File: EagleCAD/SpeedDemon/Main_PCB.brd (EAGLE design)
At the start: 77 x 46.5 mm, 65 parts, among them Q1 DMC2700, U3 LM3676, U4 STM32F072-LQFP48, X1 32.768kHz

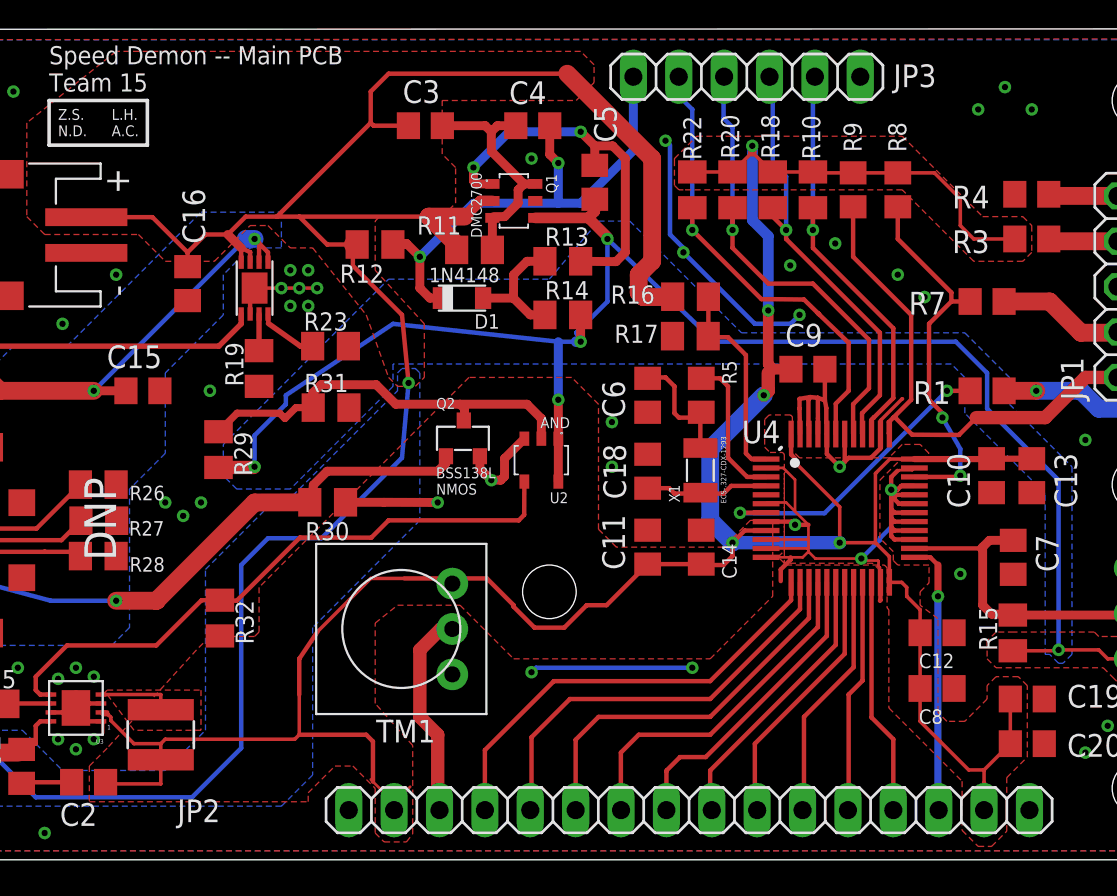
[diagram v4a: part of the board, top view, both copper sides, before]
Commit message: updated schematic/layout with pwr inlet debounce circuit and added center switch connectivity to MCU. Other small organizational changes.
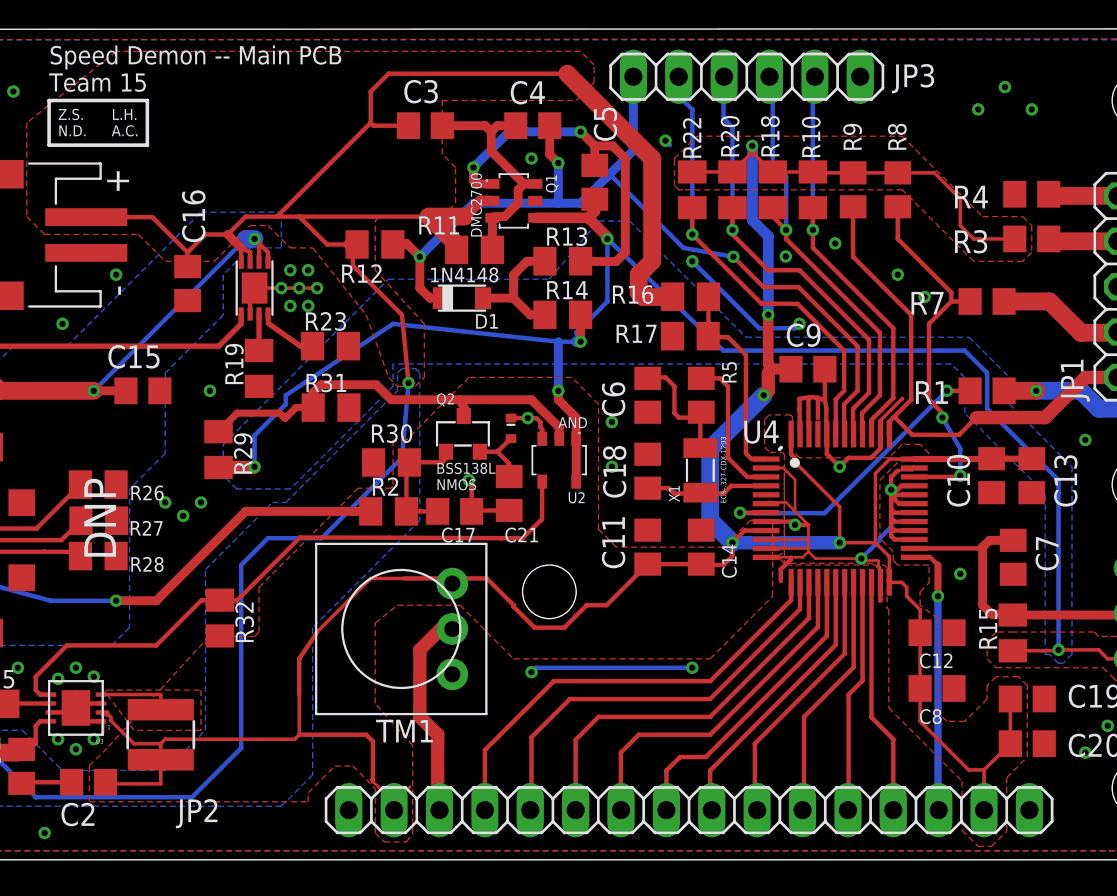
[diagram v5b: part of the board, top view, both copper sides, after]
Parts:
- added C17: 10uF, 0805_generics:C_0805
- added C21: 4.7uF, 0805_generics:C_0805
- added D3: (no value), LCRD_SMD_generics:SOD-882
- added R2: 22k, 0805_generics:R_0805
- R30: value 10k -> 82k
- moved R30 4.21 mm to (31.2, 22.2), turned to 180 degrees
- moved U2 1.00 mm to (40.5, 22.4)
- moved Q2 0.25 mm to (35.2, 23.8)
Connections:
- new net N$12: C17.1, Q2.1, R2.2, R30.1
- new net N$16: C21.1, D3.P$1, Q2.2
- net +V+_CHG: now also R2.1; no longer Q2.1, R30.1
- net GND: now also C17.2, C21.2, D3.P$2; no longer Q2.2, U4.42
- net PWR_SW: now also U4.42
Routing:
- net PWR_SW: track 28.1 -> 51.1 mm, vias 2 -> 3
- net GND: track 113.4 -> 99.9 mm
- net N$12: track 0.00 -> 7.08 mm
- net +V+_CHG: track 71.8 -> 65.7 mm
- net N$16: track 0.00 -> 3.70 mm
- net +3V3: track 163.8 -> 165.1 mm
- net BATT_CHG_LOGIC_OP: track 34.7 -> 35.8 mm
- net N$28: track 22.9 -> 23.9 mm

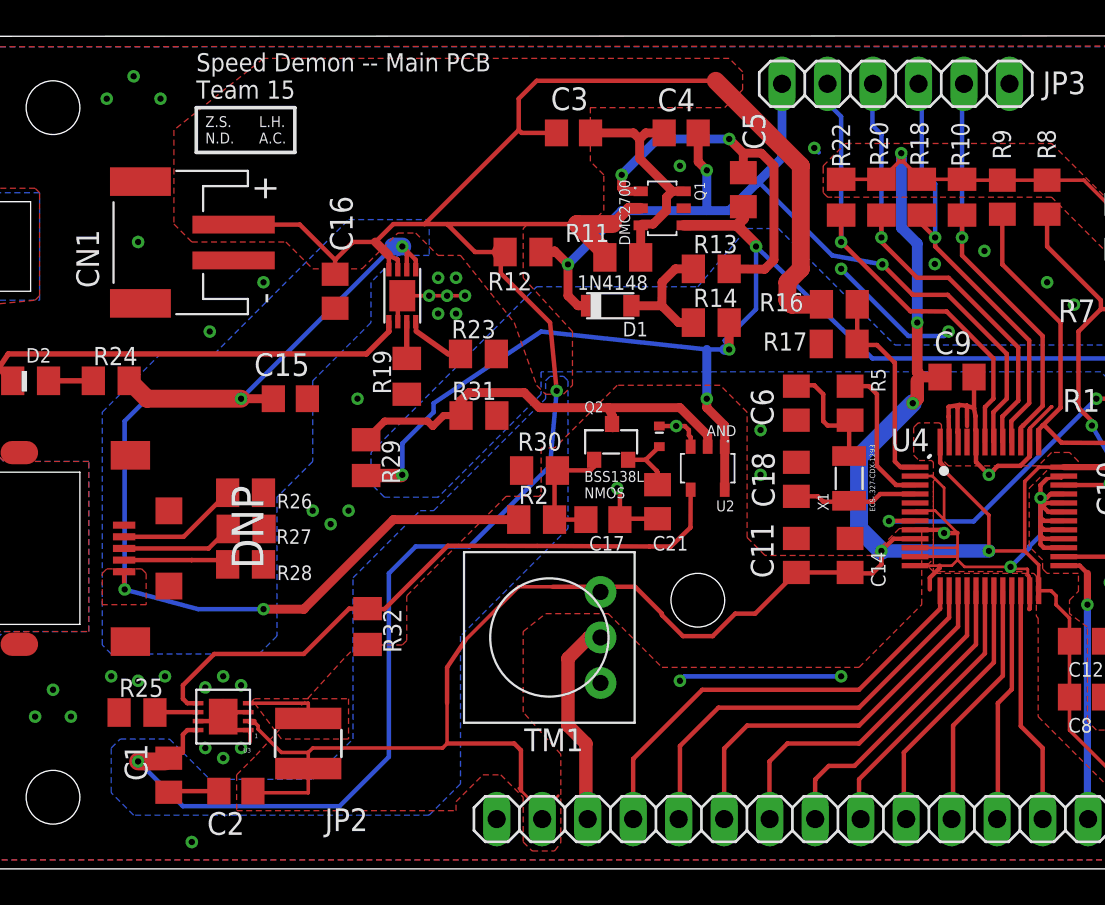
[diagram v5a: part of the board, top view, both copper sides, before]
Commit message: Changed layout to maximize distance between power inductor and everything else
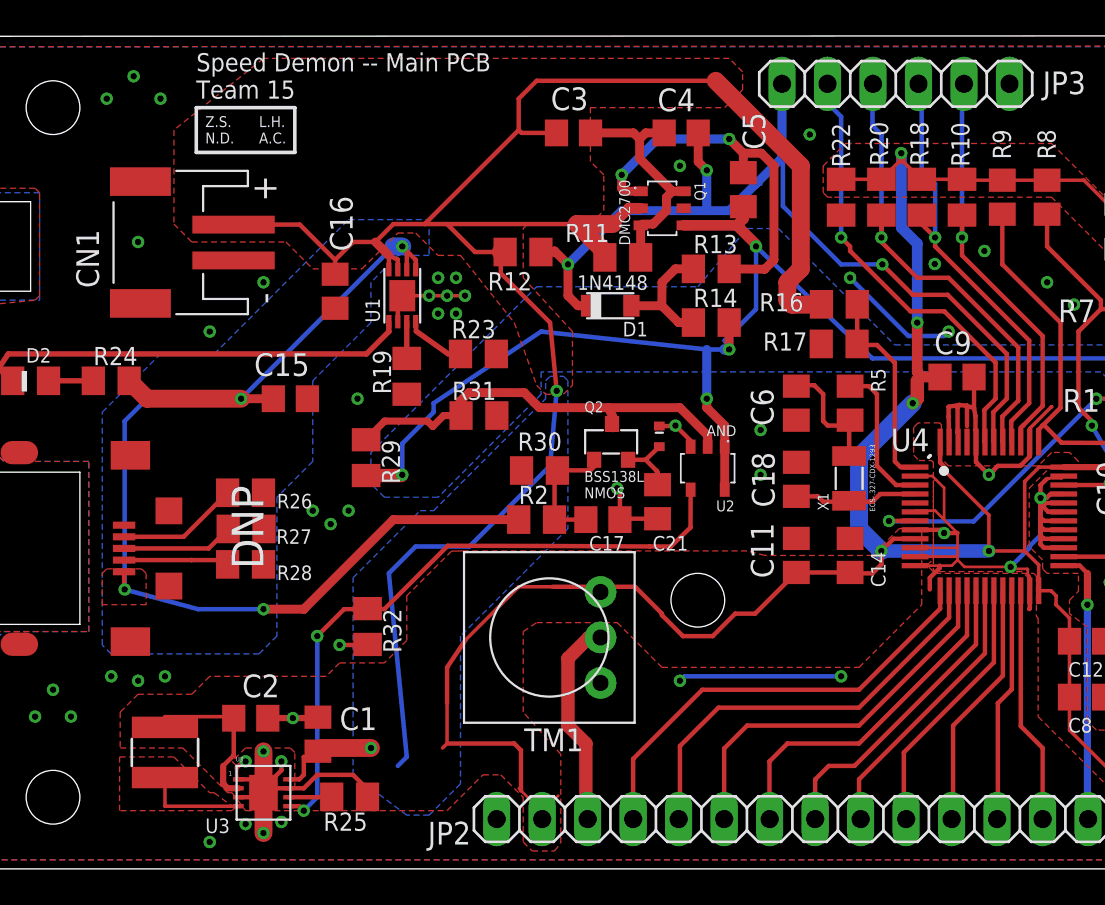
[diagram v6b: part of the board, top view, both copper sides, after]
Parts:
- moved R25 12.8 mm to (20.6, 4.02), turned to 180 degrees
- moved C1 8.64 mm to (18.8, 7.52), turned to 90 degrees
- moved L1 8.02 mm to (10.2, 6.50), turned to 270 degrees
- moved U3 4.81 mm to (15.8, 4.25), turned to 0 degrees
- moved C2 4.15 mm to (15.0, 8.41), turned to 0 degrees
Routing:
- net VBATT+: track 129.9 -> 115.7 mm
- net GND: track 99.9 -> 113.1 mm, vias 56 -> 58
- net +3V3: track 165.1 -> 157.4 mm
- net SW_LEFT: track 28.7 -> 25.3 mm
- net N$10: track 4.20 -> 5.70 mm
- net PWR_SW: track 51.1 -> 52.2 mm
- net BATT_CHG_LOGIC_OP: track 35.8 -> 36.5 mm, vias 0 -> 2
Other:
- board text added: "U1"
- board text added: "U3"

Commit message: several small changes to layout to improve ground planing
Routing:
- net GND: vias 58 -> 61
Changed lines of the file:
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@@
 <setting verticaltext="up"/>
 </settings>
-<grid distance="0.25" unitdist="mm" unit="mm" style="lines" multiple="1" display="yes" altdistance="0.003125" altunitdist="mic" altunit="mm"/>
+<grid distance="0.25" unitdist="mm" unit="mm" style="lines" multiple="1" display="no" altdistance="0.003125" altunitdist="mic" altunit="mm"/>
 <layers>
 <layer number="1" name="Top" color="4" fill="1" visible="yes" active="yes"/>
@@
 <wire x1="54.43" y1="17.43" x2="54.5" y2="17.5" width="0.1524" layer="1"/>
 <wire x1="14.938434375" y1="5" x2="14.35" y2="5" width="0.25" layer="1"/>
-<via x="8.5" y="44.25" extent="1-16" drill="0.35"/>
+<via x="9" y="44.25" extent="1-16" drill="0.35"/>
 <via x="8.75" y="35" extent="1-16" drill="0.35"/>
 <via x="12.75" y="1.5" extent="1-16" drill="0.35"/>
@@
 <wire x1="58.53" y1="24.588575" x2="59.741425" y2="25.8" width="0.2" layer="1"/>
 <wire x1="59.741425" y1="25.8" x2="59.766275" y2="25.8" width="0.2" layer="1"/>
-<via x="7" y="43" extent="1-16" drill="0.35"/>
-<via x="10" y="43" extent="1-16" drill="0.35"/>
+<via x="7.75" y="43" extent="1-16" drill="0.35"/>
+<via x="10.5" y="43" extent="1-16" drill="0.35"/>
 <via x="64" y="42" extent="1-16" drill="0.35"/>
 <via x="67" y="42" extent="1-16" drill="0.35"/>
@@
 <via x="54" y="30" extent="1-16" drill="0.35"/>
 <via x="61" y="31.5" extent="1-16" drill="0.35"/>
-<via x="72.5" y="9" extent="1-16" drill="0.35"/>
-<via x="70" y="6" extent="1-16" drill="0.35"/>
+<via x="72.5" y="8" extent="1-16" drill="0.35"/>
+<via x="70" y="8" extent="1-16" drill="0.35"/>
 <via x="3" y="8.5" extent="1-16" drill="0.35"/>
 <via x="4" y="10" extent="1-16" drill="0.35"/>
@@
 <wire x1="21.56" y1="12.53" x2="21.53" y2="12.5" width="0.25" layer="1"/>
 <wire x1="21.53" y1="12.5" x2="20" y2="12.5" width="0.25" layer="1"/>
+<via x="33" y="23.75" extent="1-16" drill="0.35"/>
+<via x="62.5" y="33.25" extent="1-16" drill="0.35"/>
+<via x="65.25" y="29" extent="1-16" drill="0.35"/>
 </signal>
 <signal name="N$10">

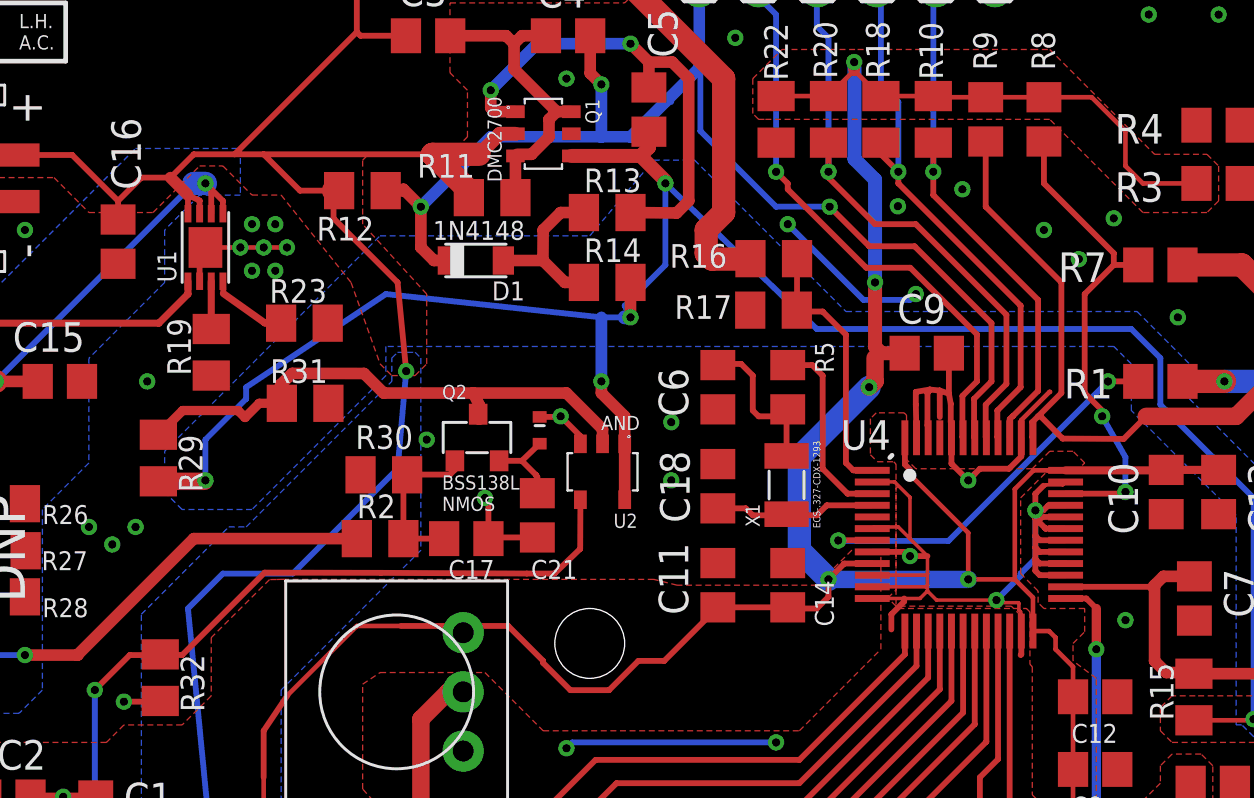
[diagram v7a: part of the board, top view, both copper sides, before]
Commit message: Added WPRs, finished changes for debounce circuit.
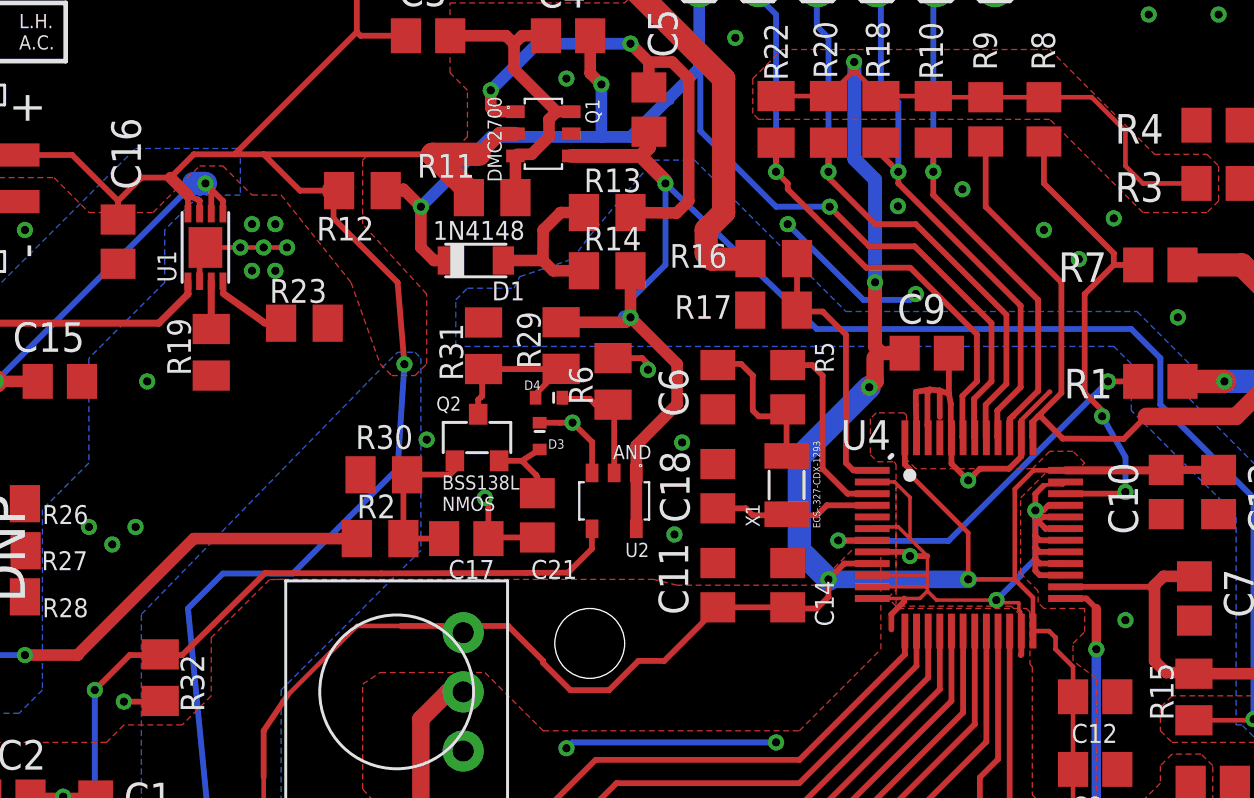
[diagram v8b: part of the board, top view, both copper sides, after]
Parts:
- added D4: (no value), LCRD_SMD_generics:SOD-882
- added R6: 1k, 0805_generics:R_0805
- moved R29 18.0 mm to (38.8, 27.8), turned to 90 degrees
- moved R31 8.05 mm to (35.4, 27.8), turned to 90 degrees
- moved U2 1.35 mm to (41.0, 21.1)
- moved R14 0.50 mm to (40.8, 31.0)
- moved D3 0.25 mm to (37.9, 23.9)
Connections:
- new net N$11: D4.P$2, R6.1, U2.2
- net GND: now also R6.2
- net N$28: now also D4.P$1; no longer U2.2
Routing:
- net VBATT+_SW: track 95.4 -> 76.9 mm, vias 5 -> 3
- net N$28: track 23.9 -> 7.06 mm
- net N$11: track 0.00 -> 5.25 mm
- net GND: track 113.1 -> 117.0 mm, vias 61 -> 62
- net SW_LEFT: track 25.3 -> 26.5 mm
- net BATT_CHG_LOGIC_OP: track 36.5 -> 35.7 mm
